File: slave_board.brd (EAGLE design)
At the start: 200 x 100 mm, 150 parts, among them IC3 ATMEGA2560-16AU, J11 1935161, J17 RJ45, J22 RJ45, J3 1935161, J6 1935161, K1 ORWH-SH-112D1F, Q1 PHB45NQ15T, Q2 PHB45NQ15T, Q3 BSS138L, Q5 BSS138L, Q7 PHB45NQ15T, Q8 IRFR9024TRPBF, U1 VNQ5E160KTR-E, U2 PCA9615, U3 INA213AIDCKT, U4 VNH7070ASTR, U5 VNH7070ASTR, U6 VNQ5E160KTR-E, U7 INA213AIDCKT, U8 LM340MP-5.0/NOPB, U9 LM340MP-5.0/NOPB, Y1 ABLS-16.000MHZ-B4-T

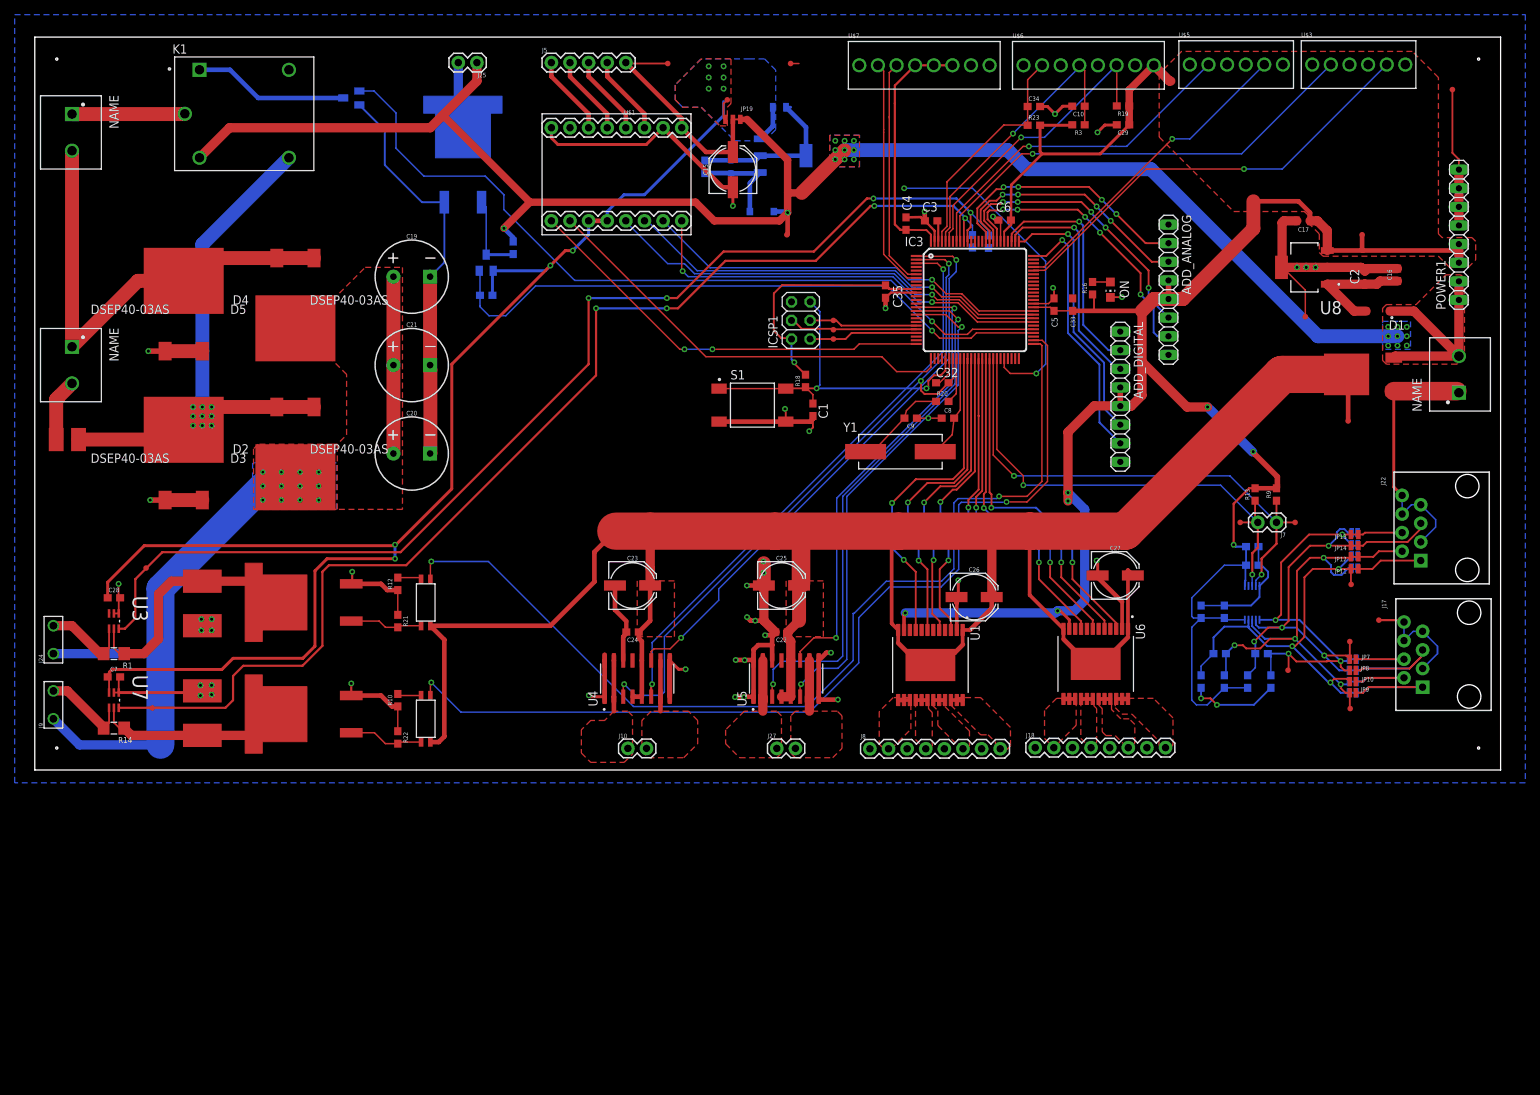
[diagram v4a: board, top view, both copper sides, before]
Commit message: More screw terminals
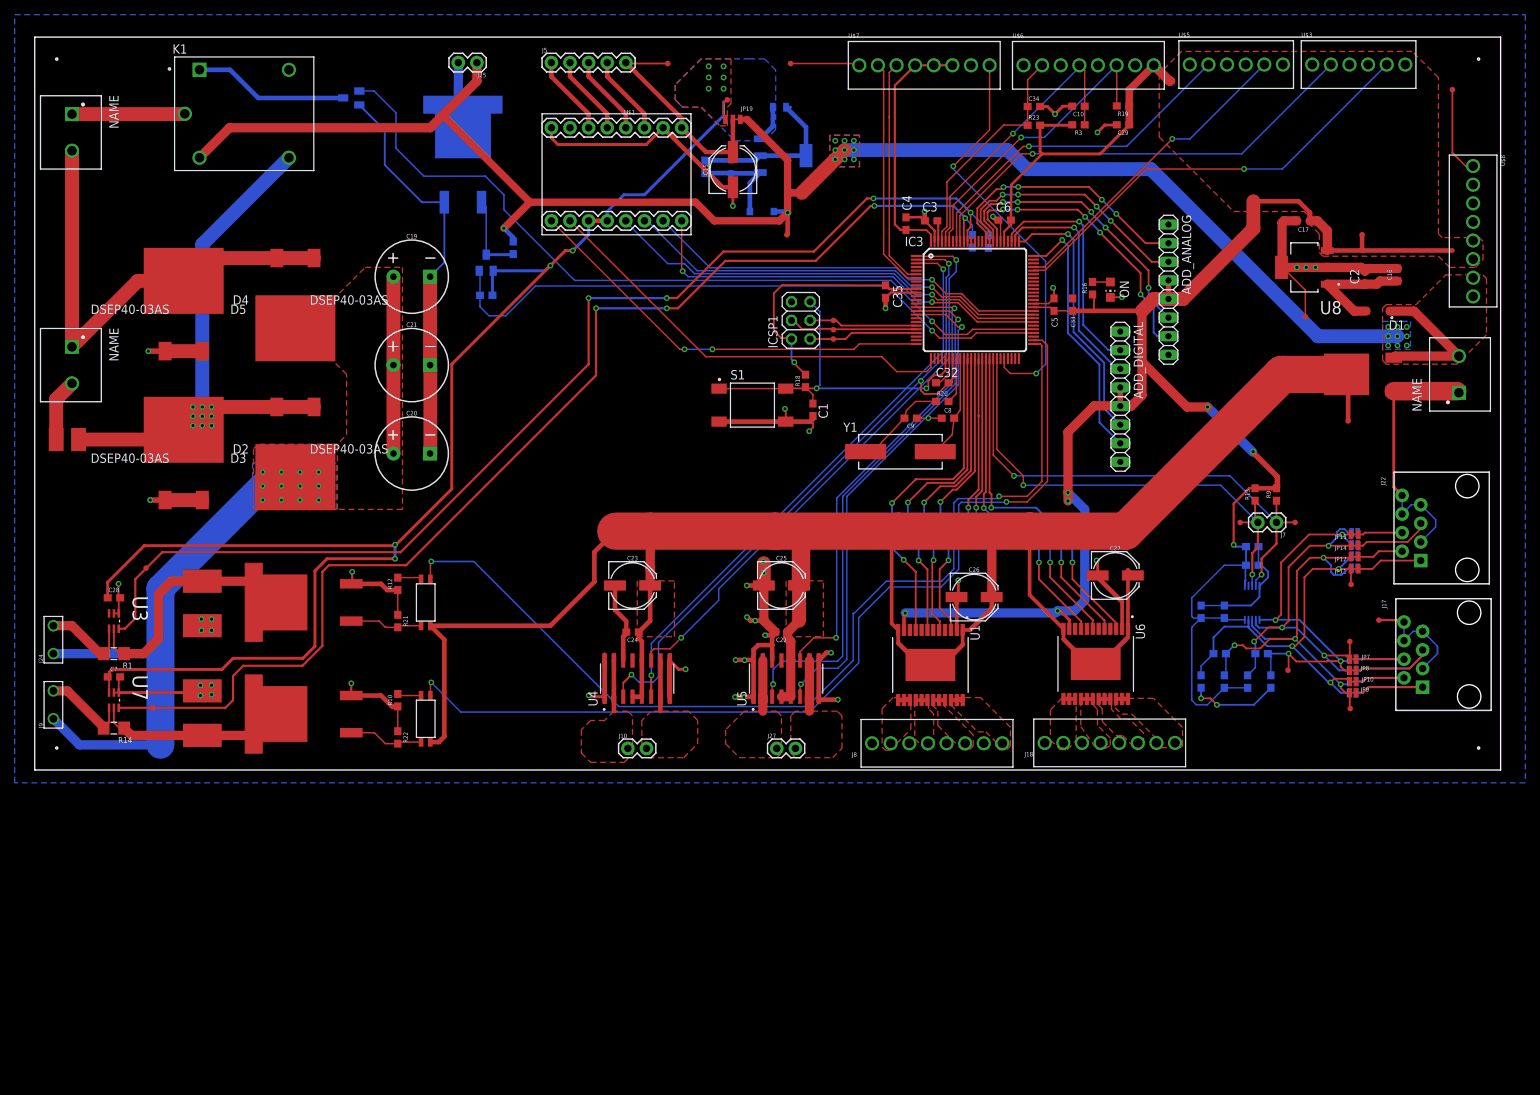
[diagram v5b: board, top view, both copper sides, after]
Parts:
- removed POWER1: 8x1F-H8.5, SmartPrj:1X08
- added U$8: OSTVN08A150, smoothio:8PIN_SCREW_TERMINAL
- J18, J8: value (none) -> OSTVN08A150; device SparkFun-Connectors:1X08 -> smoothio:8PIN_SCREW_TERMINAL
- moved J8 2.77 mm to (112.7, 0.40)
- moved J18 2.61 mm to (136.3, 0.45)
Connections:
- net +12V: now also U$8.7, U$8.8; no longer POWER1.1, POWER1.2
- net +5V: now also U$8.5, U$8.6; no longer POWER1.3, POWER1.4
- net GND: now also U$8.1, U$8.2, U$8.3, U$8.4; no longer POWER1.5, POWER1.6, POWER1.7, POWER1.8
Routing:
- net ELEV_ENC_OUT: track 45.2 -> 55.8 mm
- net +12V: track 253.8 -> 243.6 mm
- net +5V: track 371.2 -> 367.4 mm
- net PIVOT_INA: track 87.3 -> 85.3 mm
- net GND: track 463.1 -> 464.7 mm

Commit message: board progress
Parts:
- added H1, H2, H3, H4: MOUNT-HOLE3.3, holes:3,3
- moved TP1 101.1 mm to (98.0, 67.6)
- moved TP20 94.1 mm to (98.1, 72.1)
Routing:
- net +5V: track 367.4 -> 414.7 mm, vias 8 -> 10
- net N$5: track 10.8 -> 20.4 mm
- net GND: track 464.7 -> 474.0 mm
- net N$24: track 8.98 -> 18.0 mm
- net N$23: track 6.28 -> 12.6 mm
- net N$19: track 6.07 -> 12.1 mm
- net V-5_LOAD: track 202.1 -> 204.4 mm
- net CURR_SENS0: track 163.6 -> 165.6 mm
- net CURR_SENS1: track 157.9 -> 159.4 mm
- net RESET: track 49.5 -> 48.4 mm, vias 2 -> 1
- net V-STEPPER: track 30.6 -> 31.7 mm
- net ELEV_OUT_B: track 8.32 -> 7.62 mm

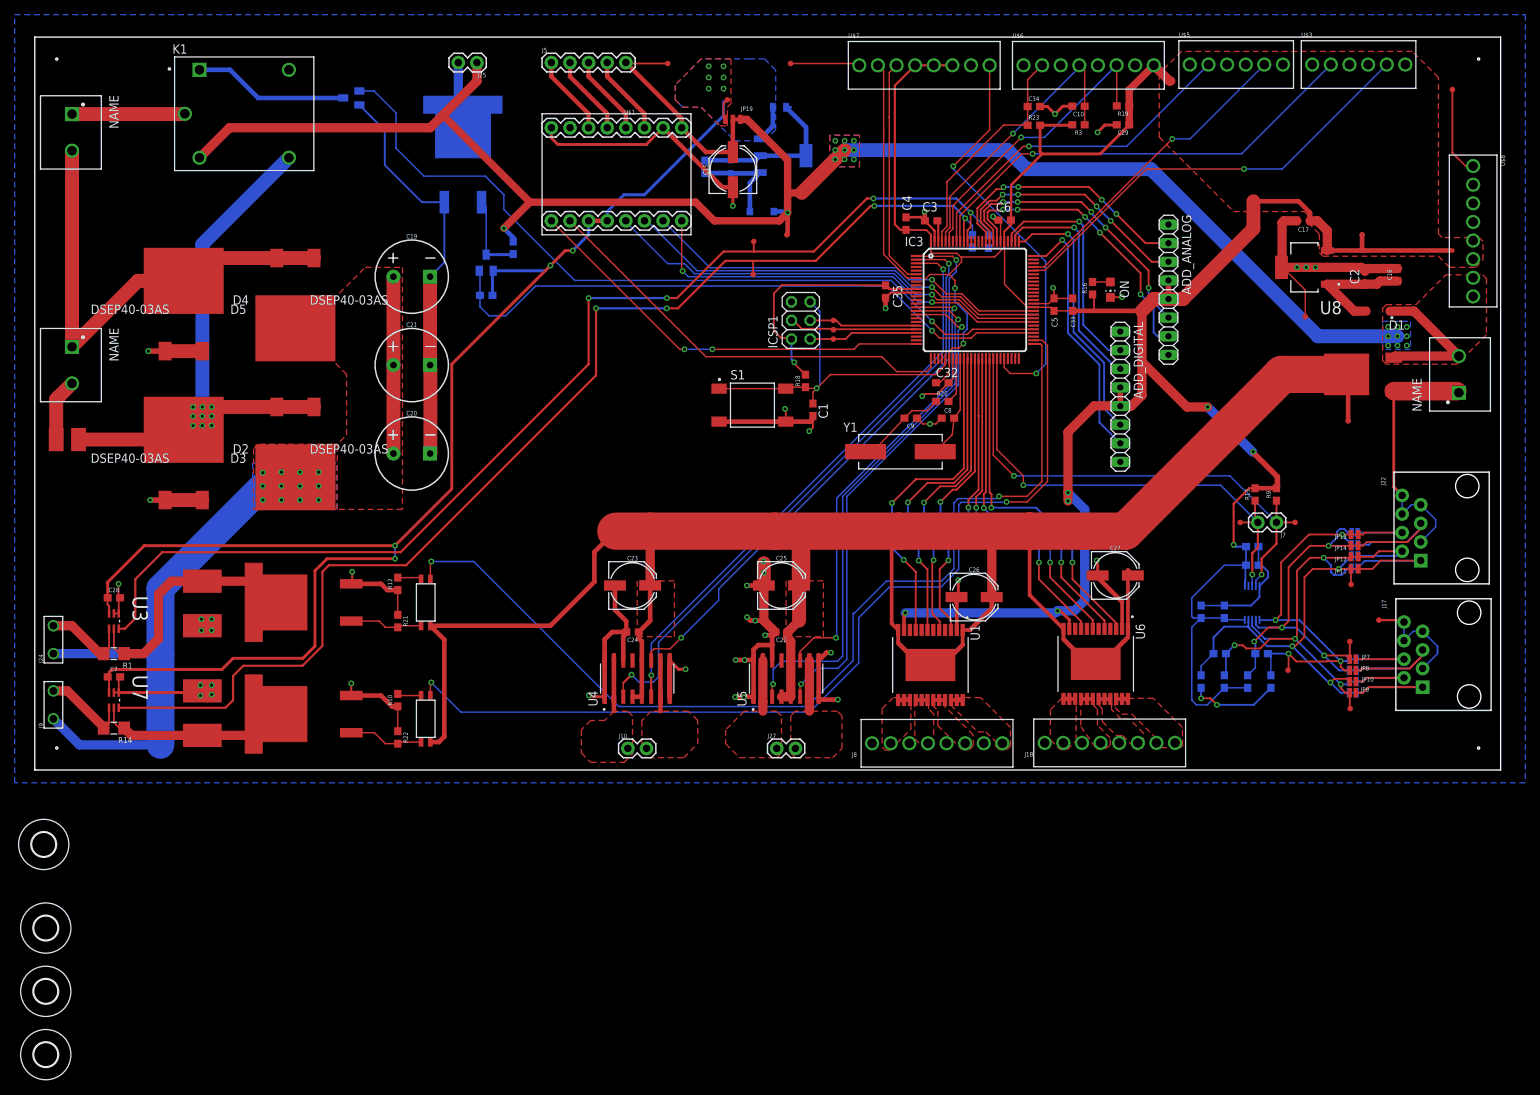
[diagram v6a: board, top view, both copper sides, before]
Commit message: Fixed silkscreen
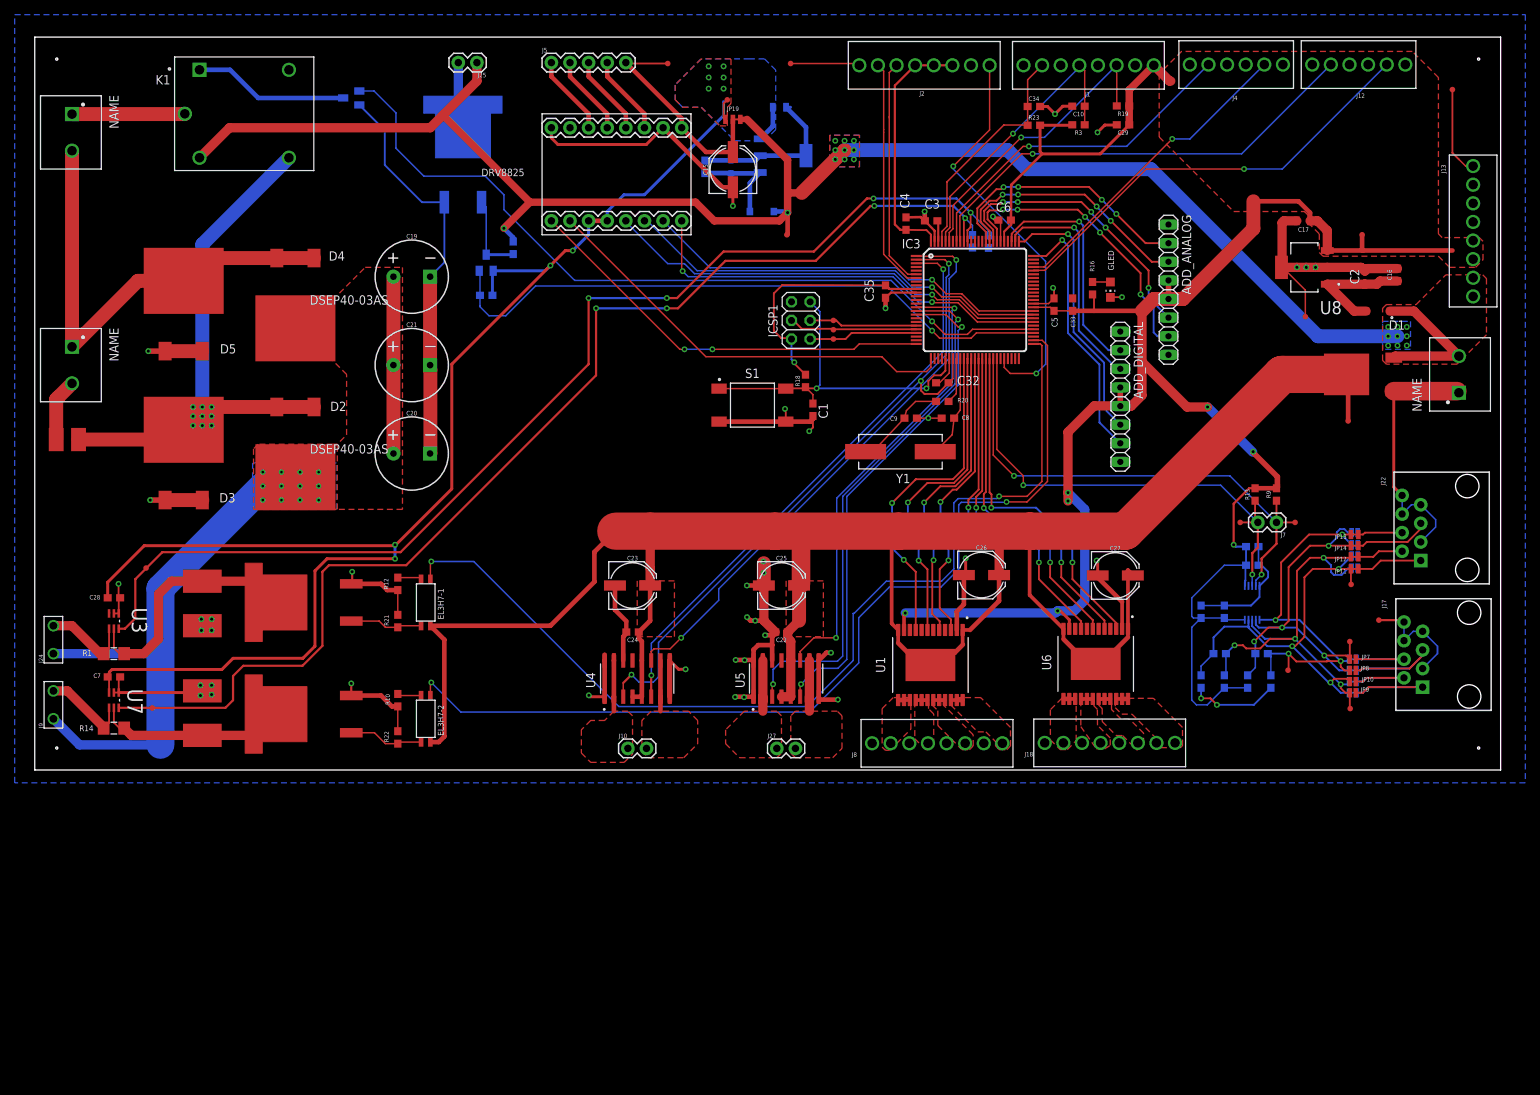
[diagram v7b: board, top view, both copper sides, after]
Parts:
- removed H1, H2, H3, H4: MOUNT-HOLE3.3, holes:3,3
- moved TP1 101.1 mm to (16.0, 8.46)
- moved TP20 94.1 mm to (15.2, 27.6)
- moved C26 3.16 mm to (129.2, 26.6)
- renumbered ON to GLED, U$1 to DRV8825, U$2 to EL3H7-2, U$3 to J12, U$4 to EL3H7-1, U$5 to J4, U$6 to J1, U$7 to J2, U$8 to J13
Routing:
- net +5V: track 414.7 -> 367.4 mm, vias 10 -> 8
- net N$5: track 20.4 -> 10.8 mm
- net N$24: track 18.0 -> 8.98 mm
- net N$23: track 12.6 -> 6.28 mm
- net N$19: track 12.1 -> 6.07 mm
- net GND: track 474.0 -> 468.1 mm
- net V-5_LOAD: track 204.4 -> 202.1 mm
- net CURR_SENS0: track 165.6 -> 163.6 mm
- net CURR_SENS1: track 159.4 -> 157.9 mm
- net RESET: track 48.4 -> 49.5 mm, vias 1 -> 2
- net V-STEPPER: track 31.7 -> 30.6 mm
- net ELEV_OUT_B: track 7.62 -> 8.32 mm

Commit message: Added mounting holes, logo
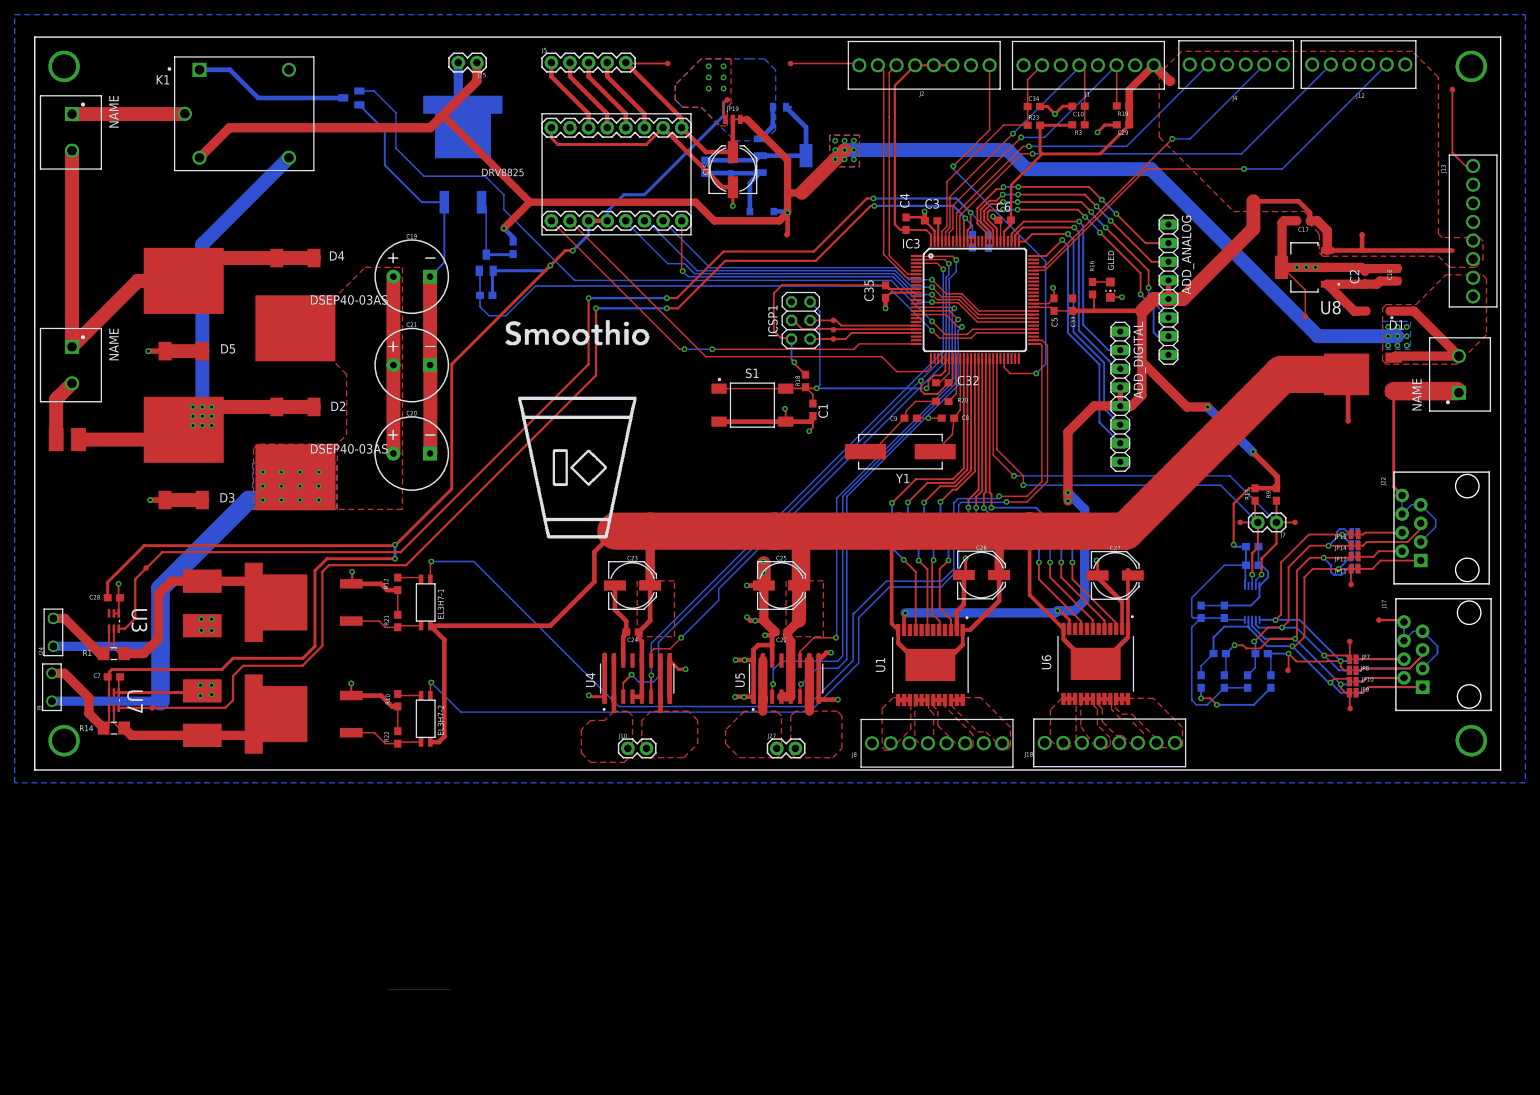
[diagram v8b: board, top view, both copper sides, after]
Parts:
- moved J9 2.41 mm to (2.34, 9.38)
- moved J24 1.00 mm to (2.54, 16.9)
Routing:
- net V-HVDC: track 98.1 -> 90.1 mm
- net BLENDER1-: track 12.1 -> 14.4 mm
- net GND: vias 46 -> 50
